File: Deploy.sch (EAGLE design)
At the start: 32 parts, among them SW5 THAU13-AB-R, SW6 THAU13-AB-R, SW7 TVAF06-A020B-R, SW8 TVAF06-A020B-R, U4 OPA340N, U5 DRIVER-LV8548MC-AH(SOIC10), U6 I-02247_NJM2845

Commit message: Deploy unit
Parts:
- added FET1, FET2: FDS4935A, mosfets:FDS4935A
- added RN1, RN2, RN3: 10k, resistor-dil:4R-N0402ARV341
- added T2, T3: HN1C01FU, transistors:HN1C01FU
- renumbered LED4 to LED2, LED5 to LED1, LED6 to LED3
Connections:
- removed net I2C_SCL: U$2.IO22
- removed net I2C_SDA: U$2.IO21
- removed net SPI_CLK: U$2.IO18
- removed net SPI_CS: U$2.IO5
- removed net SPI_MISO: U$2.IO19
- new net C1: RN3A.1, U$2.IO21
- new net C2: RN3B.1, U$2.IO19
- new net C3: RN3C.1, U$2.IO18
- new net C4: RN3D.1, U$2.IO5
- new net D1: FET1G$1.D
- new net D2: FET1G$2.D
- new net D3: FET2G$1.D
- new net D4: FET2G$2.D
- new net N$1: FET1G$1.G, RN1D.2, T2G$1.C
- new net N$13: FET2G$1.G, RN2D.2, T3G$1.C
- new net N$14: FET2G$2.G, RN2A.2, T3G$2.C
- new net N$15: RN2C.2, RN3D.2, T3G$2.B
- new net N$2: FET1G$2.G, RN1A.2, T2G$2.C
- new net N$3: RN1B.2, RN3A.2, T2G$1.B
- new net N$4: RN1C.2, RN3B.2, T2G$2.B
- new net N$7: RN2B.2, RN3C.2, T3G$1.B
- new net S1: U$2.SENSR_VP
- new net S2: U$2.SENSR_VN
- new net S3: U$2.IO34
- new net S4: U$2.IO23
- net GND: now also RN1B.1, RN1C.1, RN2B.1, RN2C.1, T2G$1.E, T2G$2.E, T3G$1.E, T3G$2.E
- net VCC: now also FET1G$1.S, FET1G$2.S, FET2G$1.S, FET2G$2.S, RN1A.1, RN1D.1, RN2A.1, RN2D.1

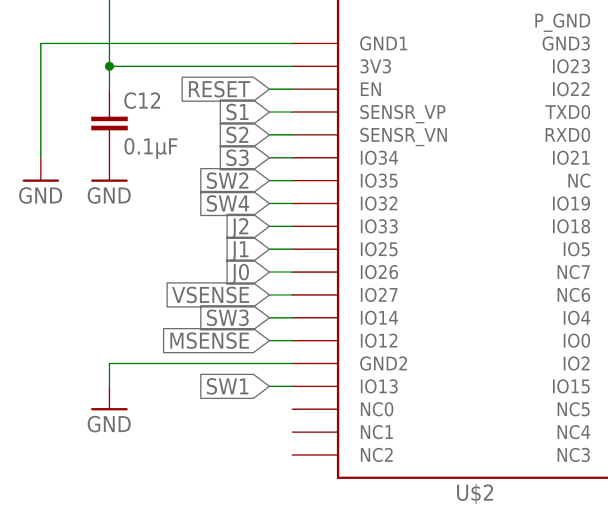
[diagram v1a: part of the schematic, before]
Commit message: Fix analog input pins
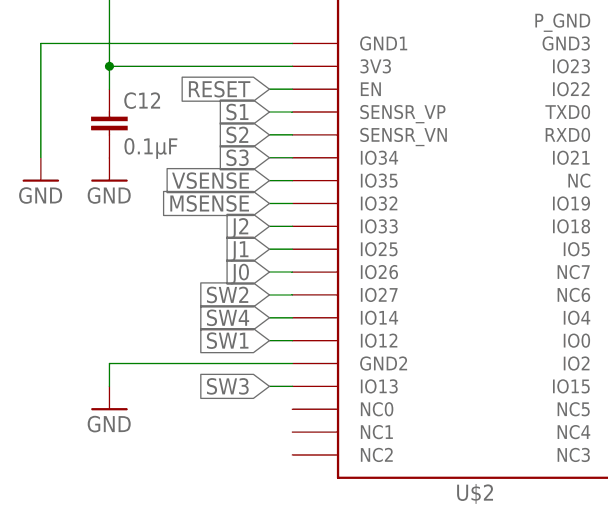
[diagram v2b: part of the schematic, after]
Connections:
- net MSENSE: now also U$2.IO32; no longer U$2.IO12
- net SW1: now also U$2.IO12; no longer U$2.IO13
- net SW2: now also U$2.IO27; no longer U$2.IO35
- net SW3: now also U$2.IO13; no longer U$2.IO14
- net SW4: now also U$2.IO14; no longer U$2.IO32
- net VSENSE: now also U$2.IO35; no longer U$2.IO27
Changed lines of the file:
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@@
 </segment>
 <segment>
-<pinref part="U$2" gate="G$1" pin="IO12"/>
-<wire x1="30.48" y1="17.78" x2="27.94" y2="17.78" width="0.1524" layer="91"/>
-<label x="27.94" y="17.78" size="1.778" layer="95" rot="R180" xref="yes"/>
+<pinref part="U$2" gate="G$1" pin="IO32"/>
+<wire x1="30.48" y1="33.02" x2="27.94" y2="33.02" width="0.1524" layer="91"/>
+<label x="27.94" y="33.02" size="1.778" layer="95" rot="R180" xref="yes"/>
 </segment>
 </net>
@@
 </segment>
 <segment>
-<pinref part="U$2" gate="G$1" pin="IO27"/>
-<wire x1="30.48" y1="22.86" x2="27.94" y2="22.86" width="0.1524" layer="91"/>
-<label x="27.94" y="22.86" size="1.778" layer="95" rot="R180" xref="yes"/>
+<pinref part="U$2" gate="G$1" pin="IO35"/>
+<wire x1="30.48" y1="35.56" x2="27.94" y2="35.56" width="0.1524" layer="91"/>
+<label x="27.94" y="35.56" size="1.778" layer="95" rot="R180" xref="yes"/>
 </segment>
 </net>
@@
 </segment>
 <segment>
-<pinref part="U$2" gate="G$1" pin="IO35"/>
-<wire x1="30.48" y1="35.56" x2="27.94" y2="35.56" width="0.1524" layer="91"/>
-<label x="27.94" y="35.56" size="1.778" layer="95" rot="R180" xref="yes"/>
+<pinref part="U$2" gate="G$1" pin="IO27"/>
+<wire x1="30.48" y1="22.86" x2="27.94" y2="22.86" width="0.1524" layer="91"/>
+<label x="27.94" y="22.86" size="1.778" layer="95" rot="R180" xref="yes"/>
 </segment>
 </net>
@@
 </segment>
 <segment>
+<pinref part="U$2" gate="G$1" pin="IO13"/>
+<wire x1="30.48" y1="12.7" x2="27.94" y2="12.7" width="0.1524" layer="91"/>
+<label x="27.94" y="12.7" size="1.778" layer="95" rot="R180" xref="yes"/>
+</segment>
+</net>
+<net name="SW4" class="0">
+<segment>
+<pinref part="SW8" gate="G$1" pin="A"/>
+<wire x1="218.44" y1="83.82" x2="215.9" y2="83.82" width="0.1524" layer="91"/>
+<label x="215.9" y="83.82" size="1.778" layer="95" rot="R180" xref="yes"/>
+</segment>
+<segment>
 <pinref part="U$2" gate="G$1" pin="IO14"/>
 <wire x1="30.48" y1="20.32" x2="27.94" y2="20.32" width="0.1524" layer="91"/>
@@
 </segment>
 </net>
-<net name="SW4" class="0">
-<segment>
-<pinref part="SW8" gate="G$1" pin="A"/>
-<wire x1="218.44" y1="83.82" x2="215.9" y2="83.82" width="0.1524" layer="91"/>
-<label x="215.9" y="83.82" size="1.778" layer="95" rot="R180" xref="yes"/>
-</segment>
-<segment>
-<pinref part="U$2" gate="G$1" pin="IO32"/>
-<wire x1="30.48" y1="33.02" x2="27.94" y2="33.02" width="0.1524" layer="91"/>
-<label x="27.94" y="33.02" size="1.778" layer="95" rot="R180" xref="yes"/>
-</segment>
-</net>
 <net name="SW1" class="0">
 <segment>
@@
 </segment>
 <segment>
-<pinref part="U$2" gate="G$1" pin="IO13"/>
-<wire x1="30.48" y1="12.7" x2="27.94" y2="12.7" width="0.1524" layer="91"/>
-<label x="27.94" y="12.7" size="1.778" layer="95" rot="R180" xref="yes"/>
-</segment>
-</net>
+<pinref part="U$2" gate="G$1" pin="IO12"/>
+<wire x1="30.48" y1="17.78" x2="27.94" y2="17.78" width="0.1524" layer="91"/>
+<label x="27.94" y="17.78" size="1.778" layer="95" rot="R180" xref="yes"/>
+</segment>
+</net>

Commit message: reduce switch pins
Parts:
- removed J3, J4, J5: (no value), jumper:SJ
- removed LED1, LED2, LED3: SK6812MINI, leds:SK6812MINI
- removed R10, R8: 1k, rcl:R-US_R0603
- removed R11, R9: 100k, rcl:R-US_R0603
- removed R12: 200k, rcl:R-US_R0603
- added LED4, LED5, LED6: SK6812MINI, leds:SK6812MINI
- added R15: 1k, rcl:R-US_R0603
- added R16, R18, R19: 100k, rcl:R-US_R0603
- added R17: 200k, rcl:R-US_R0603
- added R20, R21, R22, R23, R24: (no value), rcl:R-US_R0603
- R13: value 100k -> 1k
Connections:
- removed net J0: J3.1, U$2.IO26
- removed net J1: J4.1, U$2.IO25
- removed net J2: J5.1, U$2.IO33
- removed net N$10: R14.1, T1.G, U$4.A
- removed net N$11: LED1.DOUT, LED2.DIN
- removed net N$12: LED2.DOUT, LED3.DIN
- removed net N$5: HUSE1.P2, R14.2, T1.S
- removed net N$8: R8.2, R9.1, U4.-IN
- removed net N$9: R10.2, R11.1, U4.+IN
- removed net SW1: SW6.A, U$2.IO12
- removed net SW2: SW5.A, U$2.IO27
- removed net SW3: SW7.A, U$2.IO13
- removed net SW4: SW8.A, U$2.IO14
- new net N$18: HUSE1.P2, R19.2, T1.S
- new net N$19: R13.2, R14.1, U4.-IN
- new net N$20: R15.2, R16.1, U4.+IN
- new net N$21: R19.1, T1.G, U$4.A
- new net N$22: LED4.DIN, LED5.DOUT
- new net N$23: LED4.DOUT, LED6.DIN
- new net N$24: R22.1, R23.2, SW5.A, SW7.B
- new net N$25: R21.1, R22.2, SW6.B, SW7.A
- new net N$26: R23.1, R24.2, SW5.B, SW8.A
- new net SW: R20.1, R21.2, SW6.A, U$2.IO34
- net GND: now also LED4.GND, LED5.GND, LED6.GND, R16.2, R18.1, R24.1; no longer J3.2, J4.2, J5.2, LED1.GND, LED2.GND, LED3.GND, R11.2, R8.1, SW5.B, SW6.B, SW7.B
- net LED: now also LED5.DIN; no longer LED1.DIN
- net MGND: now also R15.1; no longer R10.1
- net MSENSE: now also R14.2; no longer R9.2
- net S1: now also U$2.IO25; no longer U$2.SENSR_VP
- net S2: now also U$2.IO26; no longer U$2.SENSR_VN
- net S3: now also U$2.IO23; no longer U$2.IO34
- net S4: now also U$2.IO22; no longer U$2.IO23
- net VCC: now also R17.2; no longer R12.2
- net VDD: now also LED4.VDD, LED5.VDD, LED6.VDD, R20.2; no longer LED1.VDD, LED2.VDD, LED3.VDD
- net VSENSE: now also R17.1, R18.2; no longer R12.1, R13.2
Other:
- note added: "Limit Switches & Push Switches"
- note removed: "Jumper Pads"
- note removed: "Limit Switches"
- note removed: "Push Switches"
- moved on the sheet: C10, C11, C12, C7, C8, C9, HUSE1, R13, R14, RS1, SW5, SW6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

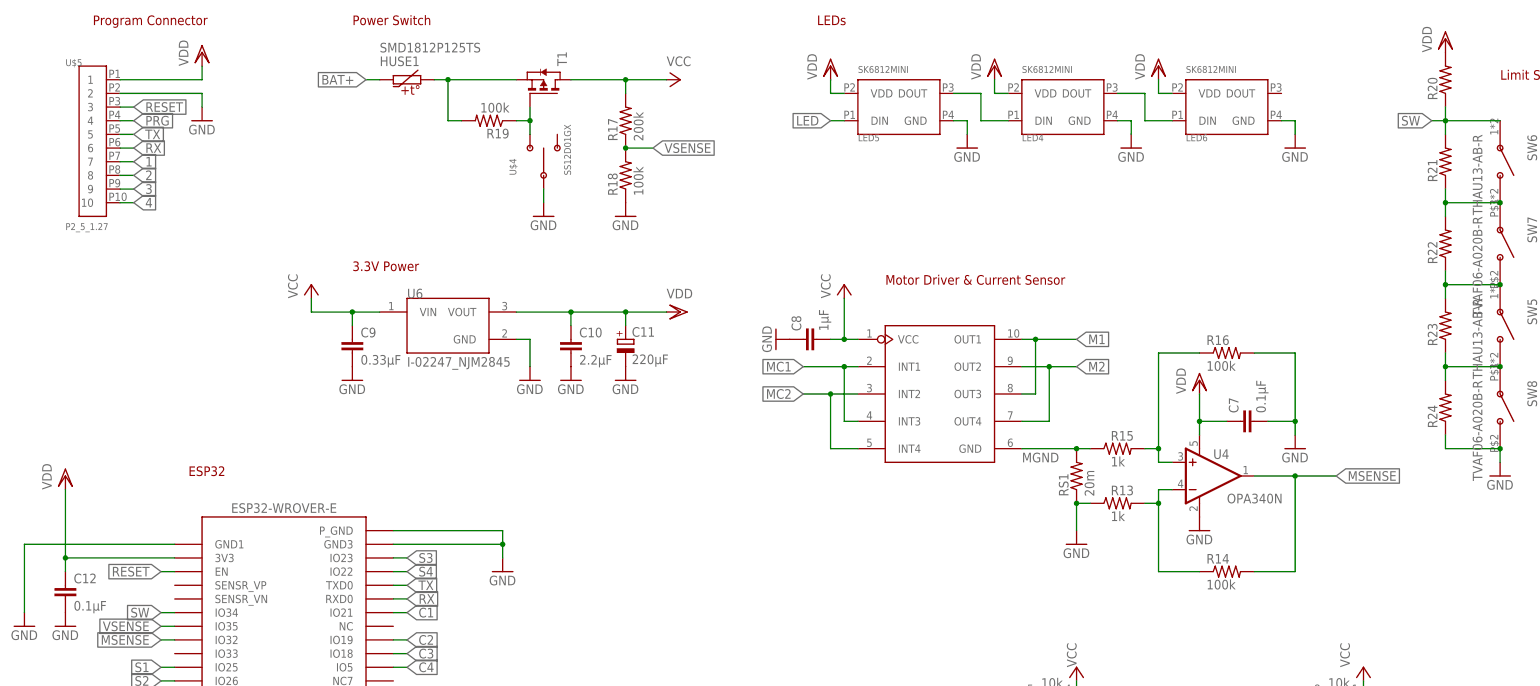
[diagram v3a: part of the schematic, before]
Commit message: change parts name
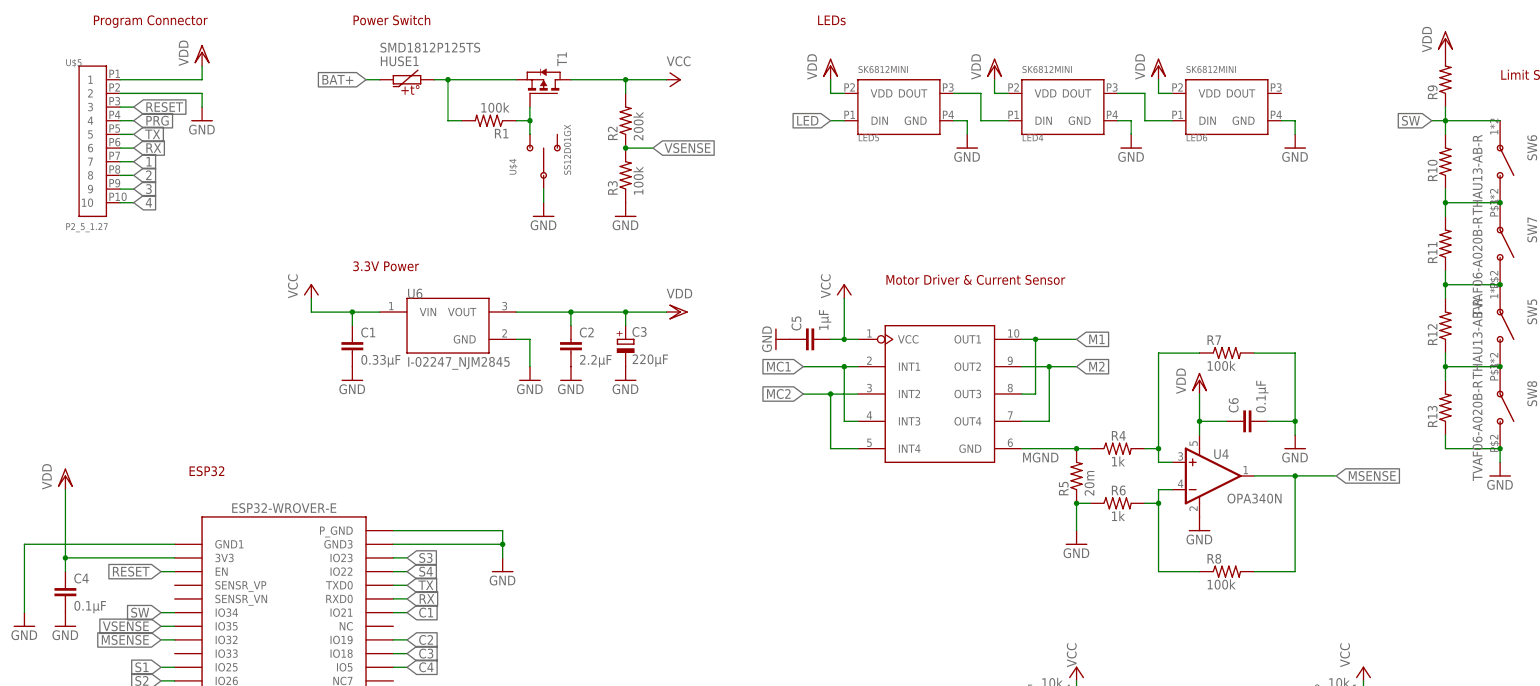
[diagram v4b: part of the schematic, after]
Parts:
- removed R24: (no value), rcl:R-US_R0603
- added R6: 1k, rcl:R-US_R0603
- R13: value 1k -> (none)
- renumbered C10 to C2, C11 to C3, C12 to C4, C7 to C6, C8 to C5, C9 to C1, R14 to R8, R15 to R4, R16 to R7, R17 to R2, R18 to R3, R19 to R1, R20 to R9, R21 to R10, R22 to R11, R23 to R12, RS1 to R5
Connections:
- net GND: now also R6.1; no longer R24.1
- net N$19: now also R6.2; no longer R13.2
- net N$26: now also R13.2; no longer R24.2
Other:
- moved on the sheet: R13
